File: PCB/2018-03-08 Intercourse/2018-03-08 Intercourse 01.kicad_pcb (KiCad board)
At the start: 2 copper layers, 85.6 x 54 mm, 49 parts, among them J1 USB_C_Receptacle, J2 TP_RST, J3 TP_TX, J4 TP_RX, J5 TP_GPIO0, J6 TP_GND1, J7 TP_GND2, J8 TP_GND3, U1 LTC3225, U2 TPS61221DCKR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

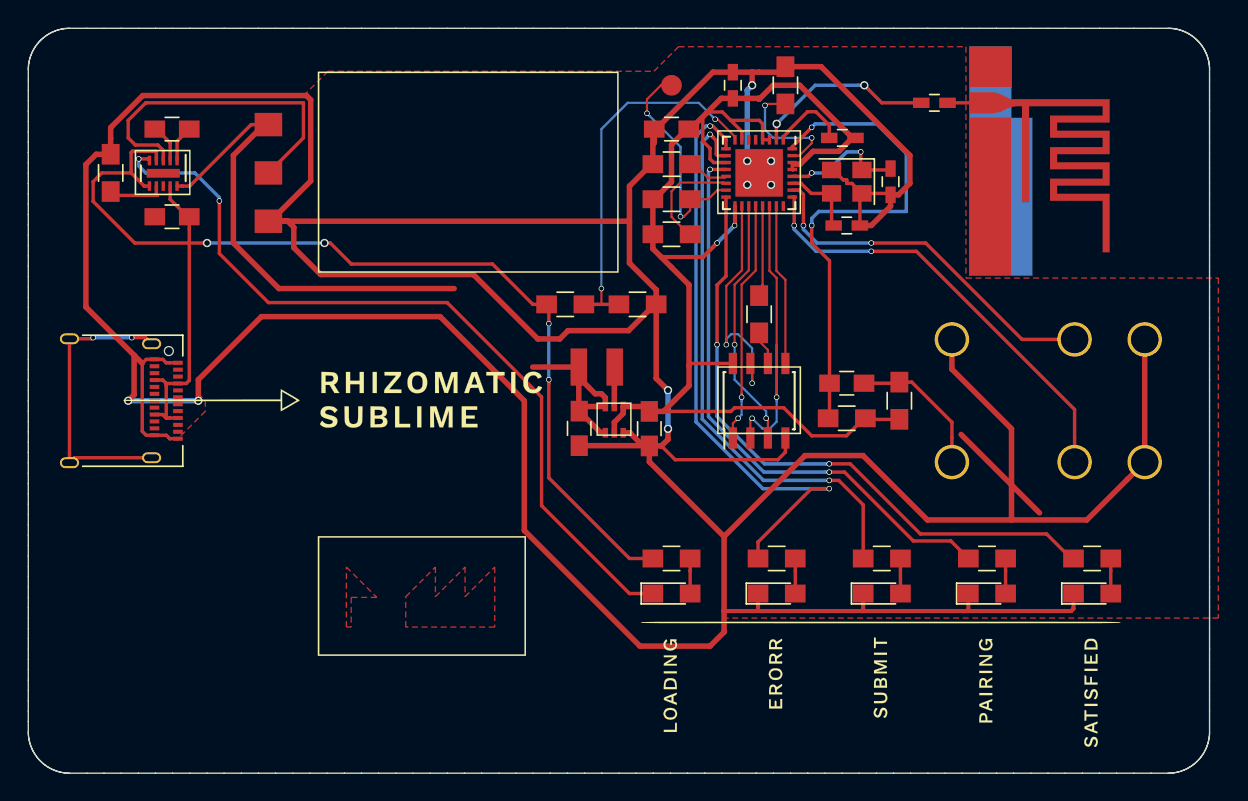
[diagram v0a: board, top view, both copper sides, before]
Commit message: FIX 2 PCBnew Errors
* Supercap + -> Henry
* SupercapCharger GND Connection
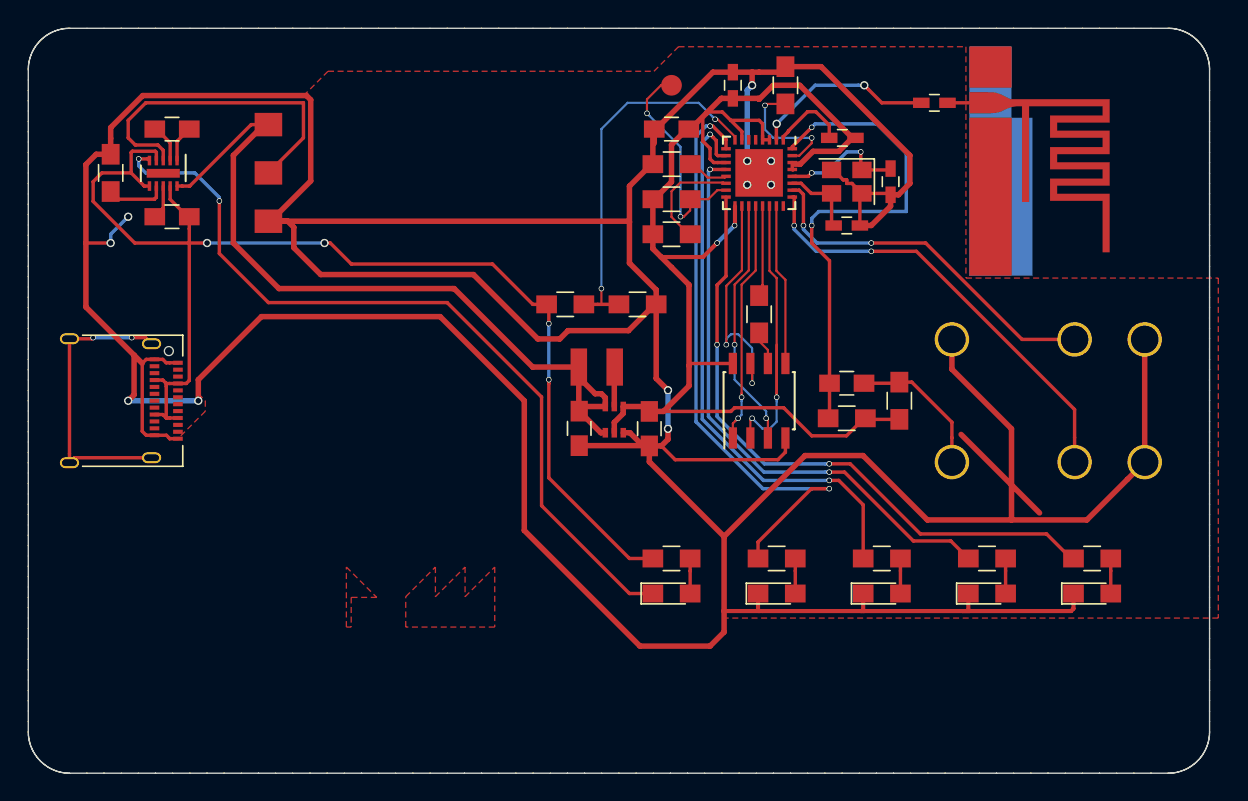
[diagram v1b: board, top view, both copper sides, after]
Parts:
- removed G***: LOGO, shapes:layout_02
- removed G***: LOGO, shapes:layout_02_back
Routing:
- net Net-(C1-Pad1): track 50.8 -> 58.9 mm
- net GND: track 393.3 -> 400.9 mm, vias 9 -> 11

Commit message: clean pcb is fine
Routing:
- net (no net): track 8.04 -> 0.00 mm
- removed copper zone on F.Cu, net (none)
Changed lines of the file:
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@@
     (links 107)
     (no_connects 0)
-    (area 101.499999 50.699999 203.300001 152.500001)
+    (area 109.549999 74.559999 195.250001 128.640001)
     (thickness 1.6)
-    (drawings 533)
-    (tracks 616)
+    (drawings 515)
+    (tracks 615)
     (zones 0)
     (modules 47)
@@
     (40 Dwgs.User user hide)
     (41 Cmts.User user hide)
-    (42 Eco1.User user hide)
+    (42 Eco1.User user)
     (43 Eco2.User user)
     (44 Edge.Cuts user)
@@
       (net 40 MODE))
   )
-  (gr_line (start 145.503109 111.544892) (end 145.503109 120.103102) (layer Eco1.User) (width 0.1))
-  (gr_line (start 130.526232 120.103102) (end 130.526232 111.544892) (layer Eco1.User) (width 0.1))
-  (gr_line (start 145.503109 120.103102) (end 130.526232 120.103102) (layer Eco1.User) (width 0.1))
-  (gr_line (start 130.526232 111.544892) (end 145.503109 111.544892) (layer Eco1.User) (width 0.1))
-  (gr_line (start 143.363555 113.684446) (end 143.363555 117.963554) (layer Eco1.User) (width 0.1))
-  (gr_line (start 139.084446 113.684446) (end 139.084446 115.824) (layer Eco1.User) (width 0.1))
-  (gr_line (start 136.944892 117.963554) (end 136.944892 115.824) (layer Eco1.User) (width 0.1))
-  (gr_line (start 132.665786 113.684437) (end 132.665786 115.823992) (layer Eco1.User) (width 0.1))
-  (gr_line (start 143.363555 117.963554) (end 136.944892 117.963554) (layer Eco1.User) (width 0.1))
-  (gr_line (start 139.084446 115.824) (end 141.224 113.684446) (layer Eco1.User) (width 0.1))
-  (gr_line (start 136.944892 115.824) (end 139.084446 113.684446) (layer Eco1.User) (width 0.1))
-  (gr_line (start 141.224 113.684446) (end 141.224 115.824) (layer Eco1.User) (width 0.1))
-  (gr_line (start 134.805341 115.823992) (end 132.665786 113.684437) (layer Eco1.User) (width 0.1))
-  (gr_line (start 132.984264 115.823992) (end 134.805341 115.823992) (layer Eco1.User) (width 0.1))
-  (gr_line (start 132.984264 117.963547) (end 132.984264 115.823992) (layer Eco1.User) (width 0.1))
-  (gr_line (start 132.665786 117.963547) (end 132.984264 117.963547) (layer Eco1.User) (width 0.1))
-  (gr_line (start 132.665786 115.823992) (end 132.665786 117.963547) (layer Eco1.User) (width 0.1))
-  (gr_line (start 141.224 115.824) (end 143.363555 113.684446) (layer Eco1.User) (width 0.1))
   (gr_line (start 121.30625 74.61) (end 122.55 74.61) (layer Edge.Cuts) (width 0.1))
   (gr_line (start 111.640465 74.768302) (end 111.710437 74.745461) (layer Edge.Cuts) (width 0.1))
@@
   (gr_line (start 101.6 101.6) (end 203.2 101.6) (layer Eco1.User) (width 0.2))
   (gr_line (start 152.4 50.8) (end 152.4 152.4) (layer Eco1.User) (width 0.2))
-  (segment (start 177.193607 104.041607) (end 182.88 109.728) (width 0.4) (layer F.Cu) (net 0))
   (segment (start 176.21 80.01) (end 178.355 80.01) (width 0.25) (layer F.Cu) (net 1))
   (segment (start 140.335 93.472) (end 140.462 93.472) (width 0.4) (layer F.Cu) (net 2))
@@
   (segment (start 129.54 80.01) (end 129.54 82.55) (width 0.25) (layer F.Cu) (net 3))
   (segment (start 129.54 82.55) (end 127 85.09) (width 0.25) (layer F.Cu) (net 3))
+  (segment (start 128.016 88.59) (end 128.4 88.59) (width 0.4) (layer F.Cu) (net 4))
+  (segment (start 155 94.615) (end 155.1 94.615) (width 0.4) (layer F.Cu) (net 4))
+  (segment (start 128.4 88.59) (end 128.839999 89.029999) (width 0.4) (layer F.Cu) (net 4))
+  (segment (start 146.853996 97.45) (end 147.786002 97.45) (width 0.4) (layer F.Cu) (net 4))
+  (segment (start 128.839999 89.029999) (end 128.839999 90.506001) (width 0.4) (layer F.Cu) (net 4))
+  (segment (start 128.839999 90.506001) (end 130.883998 92.55) (width 0.4) (layer F.Cu) (net 4))
+  (segment (start 130.883998 92.55) (end 141.953996 92.55) (width 0.4) (layer F.Cu) (net 4))
+  (segment (start 141.953996 92.55) (end 146.853996 97.45) (width 0.4) (layer F.Cu) (net 4))
+  (segment (start 147.786002 97.45) (end 148.716002 96.52) (width 0.4) (layer F.Cu) (net 4))
+  (segment (start 148.716002 96.52) (end 153.095 96.52) (width 0.4) (layer F.Cu) (net 4))
+  (segment (start 153.095 96.52) (end 155 94.615) (width 0.4) (layer F.Cu) (net 4))
   (via (at 116.84 88.265) (size 0.6) (drill 0.4) (layers F.Cu B.Cu) (net 4))
   (segment (start 113.77499 90.17) (end 115.57 90.17) (width 0.25) (layer F.Cu) (net 4))
@@
   (segment (start 162.052 77.79) (end 162.052 78.739926) (width 0.4) (layer F.Cu) (net 4))
   (segment (start 161.752001 79.039925) (end 162.052 78.739926) (width 0.4) (layer B.Cu) (net 4))
-  (segment (start 128.839999 89.029999) (end 128.839999 90.506001) (width 0.4) (layer F.Cu) (net 4))
-  (segment (start 128.839999 90.506001) (end 130.789998 92.456) (width 0.4) (layer F.Cu) (net 4))
-  (segment (start 141.859996 92.456) (end 146.523997 97.120001) (width 0.4) (layer F.Cu) (net 4))
-  (segment (start 130.789998 92.456) (end 141.859996 92.456) (width 0.4) (layer F.Cu) (net 4))
-  (segment (start 155 94.615) (end 155.1 94.615) (width 0.4) (layer F.Cu) (net 4))
-  (segment (start 148.716002 96.52) (end 153.095 96.52) (width 0.4) (layer F.Cu) (net 4))
-  (segment (start 148.116001 97.120001) (end 148.716002 96.52) (width 0.4) (layer F.Cu) (net 4))
-  (segment (start 128.016 88.59) (end 128.4 88.59) (width 0.4) (layer F.Cu) (net 4))
-  (segment (start 153.095 96.52) (end 155 94.615) (width 0.4) (layer F.Cu) (net 4))
-  (segment (start 128.4 88.59) (end 128.839999 89.029999) (width 0.4) (layer F.Cu) (net 4))
-  (segment (start 146.523997 97.120001) (end 148.116001 97.120001) (width 0.4) (layer F.Cu) (net 4))
   (segment (start 160.655 77.79) (end 162.052 77.79) (width 0.4) (layer F.Cu) (net 4))
   (segment (start 162.052 77.79) (end 162.56 77.79) (width 0.4) (layer F.Cu) (net 4))
@@
       )
     )
-  )
-  (zone (net 0) (net_name "") (layer F.Cu) (hatch edge 0.508)
-    (connect_pads (clearance 0.508))
-    (min_thickness 0.254)
-    (fill yes (arc_segments 16) (thermal_gap 0.508) (thermal_bridge_width 0.508))
-    (polygon
-      (pts
-        (xy 132.65 118) (xy 132.65 113.65) (xy 134.85 115.85) (xy 133 115.85) (xy 133 118)
-      )
-    )
-  )
-  (zone (net 0) (net_name "") (layer F.Cu) (hatch edge 0.508)
-    (connect_pads (clearance 0.508))
-    (min_thickness 0.254)
-    (fill yes (arc_segments 16) (thermal_gap 0.508) (thermal_bridge_width 0.508))
-    (polygon
-      (pts
-        (xy 136.95 118) (xy 136.95 115.8) (xy 139.1 113.65) (xy 139.1 115.8) (xy 141.25 113.65)
-        (xy 141.25 115.8) (xy 143.4 113.65) (xy 143.4 118)
-      )
-    )

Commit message: added layout and created gerber files
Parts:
- added G***: LOGO, shapes:layout_03_back, B.Cu at (152.4, 101.6)
- added G***: LOGO, shapes:layout_03_front, F.Cu at (152.4, 101.6)
- added G***: LOGO, shapes:layout_03_eco, F.Cu at (152.4, 101.6)
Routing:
- added copper zone on F.Cu, net (none)

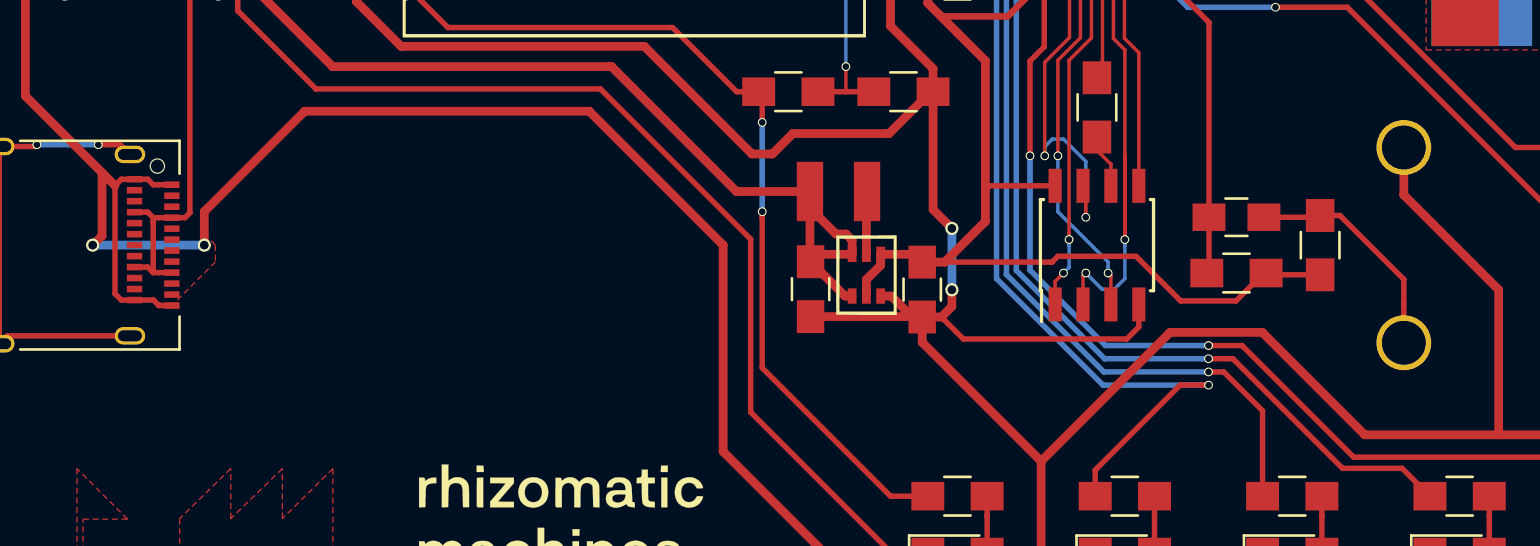
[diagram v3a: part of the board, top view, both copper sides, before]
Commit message: Add USBRST Connection on .sch & .pcb
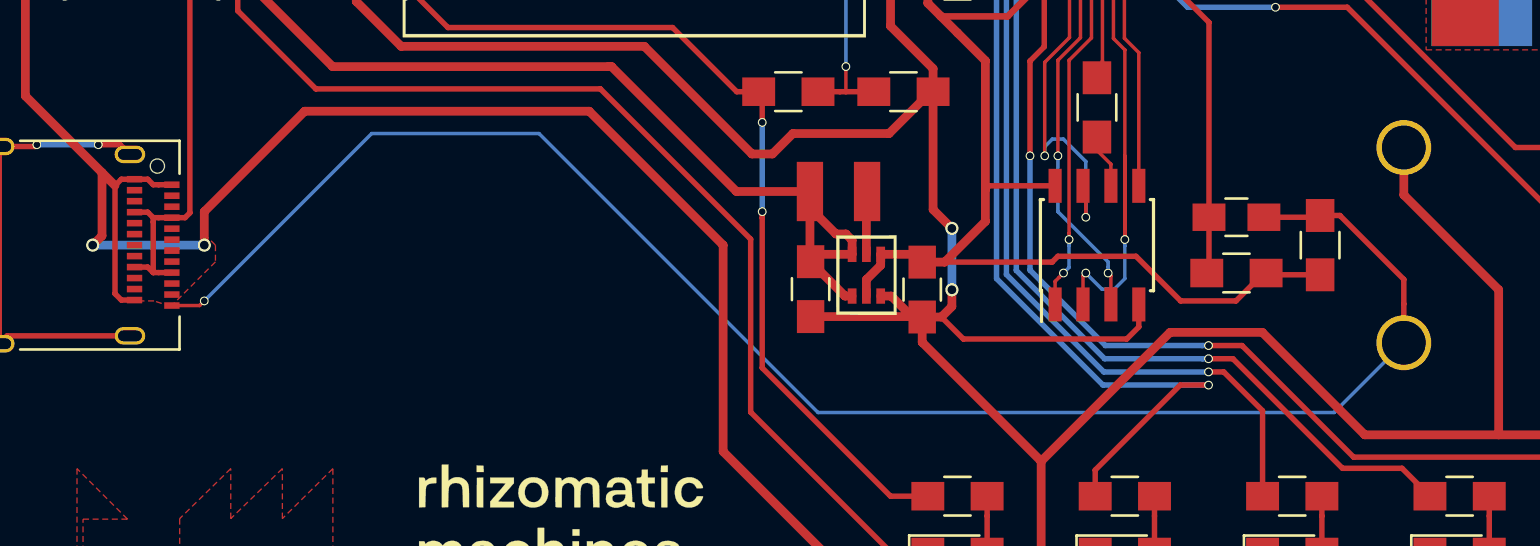
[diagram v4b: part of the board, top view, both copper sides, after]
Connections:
- C8 pad 2: Net-(C8-Pad2) -> USBRST
- J1 pad A12: GND -> USBRST
- J2 pad 1: Net-(C8-Pad2) -> USBRST
- R5 pad 2: Net-(C8-Pad2) -> USBRST
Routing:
- net USBRST: track 0.00 -> 76.5 mm, vias 0 -> 2
- net Net-(C8-Pad2): track 10.6 -> 0.00 mm
- net GND: track 401.2 -> 399.4 mm

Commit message: rev3
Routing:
- net USBRST: track 76.5 -> 77.1 mm, vias 2 -> 1
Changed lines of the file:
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@@
   (segment (start 160.181997 93.275741) (end 160.181997 97.536) (width 0.16) (layer F.Cu) (net 56))
   (via (at 160.181997 97.536) (size 0.4) (drill 0.3) (layers F.Cu B.Cu) (net 56))
-  (segment (start 120.445 104.35) (end 121.71 104.35) (width 0.16) (layer F.Cu) (net 60) (status 400000))
-  (segment (start 173.355 109.22) (end 176.53 106.045) (width 0.16) (layer B.Cu) (net 60) (status 800000))
-  (segment (start 149.86 109.22) (end 173.355 109.22) (width 0.16) (layer B.Cu) (net 60))
-  (segment (start 137.16 96.52) (end 149.86 109.22) (width 0.16) (layer B.Cu) (net 60))
-  (segment (start 129.54 96.52) (end 137.16 96.52) (width 0.16) (layer B.Cu) (net 60))
-  (segment (start 121.92 104.14) (end 129.54 96.52) (width 0.16) (layer B.Cu) (net 60))
-  (via (at 121.92 104.14) (size 0.4) (drill 0.3) (layers F.Cu B.Cu) (net 60))
-  (segment (start 121.71 104.35) (end 121.92 104.14) (width 0.16) (layer F.Cu) (net 60))
-  (via (at 176.53 106.045) (size 0.4) (drill 0.3) (layers F.Cu B.Cu) (net 60) (status C00000))
+  (segment (start 119.634 104.14) (end 121.92 104.14) (width 0.16) (layer B.Cu) (net 60))
+  (segment (start 120.445 104.35) (end 119.844 104.35) (width 0.16) (layer F.Cu) (net 60))
+  (segment (start 119.844 104.35) (end 119.634 104.14) (width 0.16) (layer F.Cu) (net 60))
+  (via (at 119.634 104.14) (size 0.4) (drill 0.3) (layers F.Cu B.Cu) (net 60))
+  (segment (start 121.92 104.14) (end 128.905 97.155) (width 0.16) (layer B.Cu) (net 60))
+  (segment (start 128.905 97.155) (end 137.795 97.155) (width 0.16) (layer B.Cu) (net 60))
+  (segment (start 173.99 108.585) (end 176.53 106.045) (width 0.16) (layer B.Cu) (net 60))
+  (segment (start 137.795 97.155) (end 149.225 108.585) (width 0.16) (layer B.Cu) (net 60))
+  (segment (start 149.225 108.585) (end 173.99 108.585) (width 0.16) (layer B.Cu) (net 60))
   (segment (start 172.72 100.25) (end 173.62 100.25) (width 0.25) (layer F.Cu) (net 60))
   (segment (start 173.62 100.25) (end 176.53 103.16) (width 0.25) (layer F.Cu) (net 60))

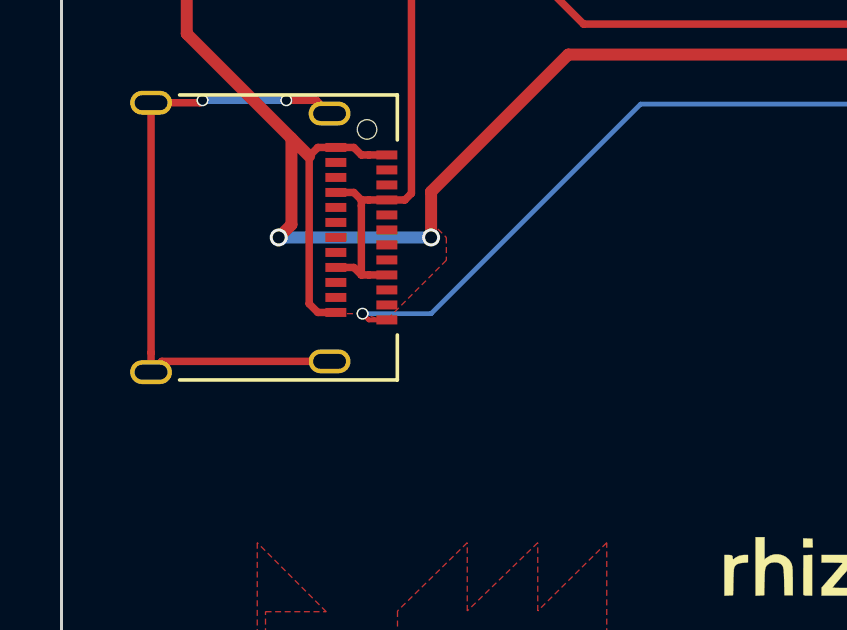
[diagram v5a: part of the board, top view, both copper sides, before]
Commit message: rev3 fixed via position
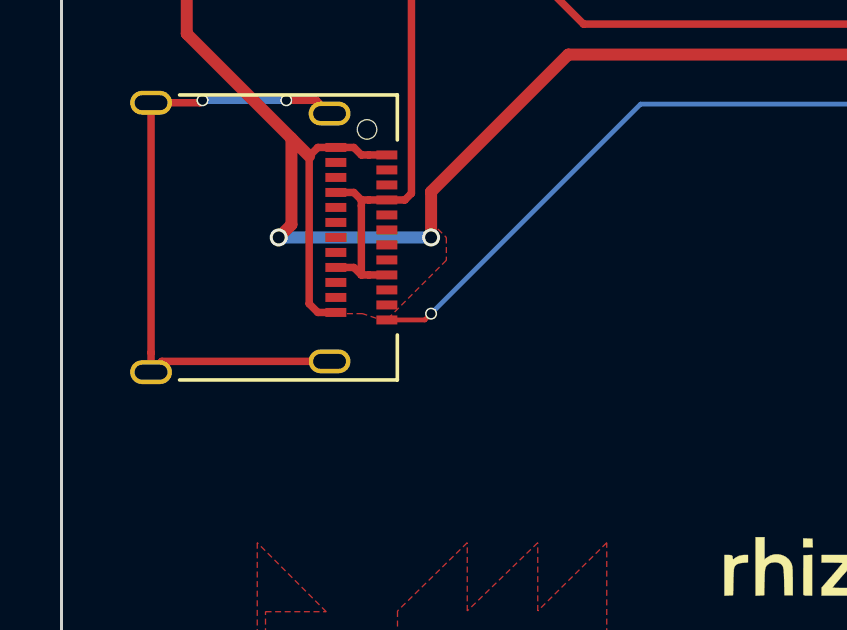
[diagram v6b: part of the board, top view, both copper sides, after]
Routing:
- net USBRST: track 77.1 -> 75.5 mm
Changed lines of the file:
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@@
     (thickness 1.6)
     (drawings 515)
-    (tracks 619)
+    (tracks 618)
     (zones 0)
     (modules 50)
@@
     (0 F.Cu signal)
     (31 B.Cu signal)
-    (32 B.Adhes user hide)
+    (32 B.Adhes user)
     (33 F.Adhes user)
     (34 B.Paste user)
@@
       (drillshape 0)
       (scaleselection 1)
-      (outputdirectory gerber/))
+      (outputdirectory gerber_rev3/))
   )
   (net 0 "")
@@
   (segment (start 160.181997 93.275741) (end 160.181997 97.536) (width 0.16) (layer F.Cu) (net 56))
   (via (at 160.181997 97.536) (size 0.4) (drill 0.3) (layers F.Cu B.Cu) (net 56))
-  (segment (start 119.634 104.14) (end 121.92 104.14) (width 0.16) (layer B.Cu) (net 60))
-  (segment (start 120.445 104.35) (end 119.844 104.35) (width 0.16) (layer F.Cu) (net 60))
-  (segment (start 119.844 104.35) (end 119.634 104.14) (width 0.16) (layer F.Cu) (net 60))
-  (via (at 119.634 104.14) (size 0.4) (drill 0.3) (layers F.Cu B.Cu) (net 60))
   (segment (start 121.92 104.14) (end 128.905 97.155) (width 0.16) (layer B.Cu) (net 60))
+  (segment (start 121.71 104.35) (end 121.92 104.14) (width 0.16) (layer F.Cu) (net 60))
+  (via (at 121.92 104.14) (size 0.4) (drill 0.3) (layers F.Cu B.Cu) (net 60))
+  (segment (start 120.445 104.35) (end 121.71 104.35) (width 0.16) (layer F.Cu) (net 60))
   (segment (start 128.905 97.155) (end 137.795 97.155) (width 0.16) (layer B.Cu) (net 60))
-  (segment (start 173.99 108.585) (end 176.53 106.045) (width 0.16) (layer B.Cu) (net 60))
   (segment (start 137.795 97.155) (end 149.225 108.585) (width 0.16) (layer B.Cu) (net 60))
   (segment (start 149.225 108.585) (end 173.99 108.585) (width 0.16) (layer B.Cu) (net 60))
+  (segment (start 173.99 108.585) (end 176.53 106.045) (width 0.16) (layer B.Cu) (net 60))
   (segment (start 172.72 100.25) (end 173.62 100.25) (width 0.25) (layer F.Cu) (net 60))
   (segment (start 173.62 100.25) (end 176.53 103.16) (width 0.25) (layer F.Cu) (net 60))
